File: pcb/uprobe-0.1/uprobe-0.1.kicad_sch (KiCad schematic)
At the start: 5 parts, among them J1 uConsoleEXT

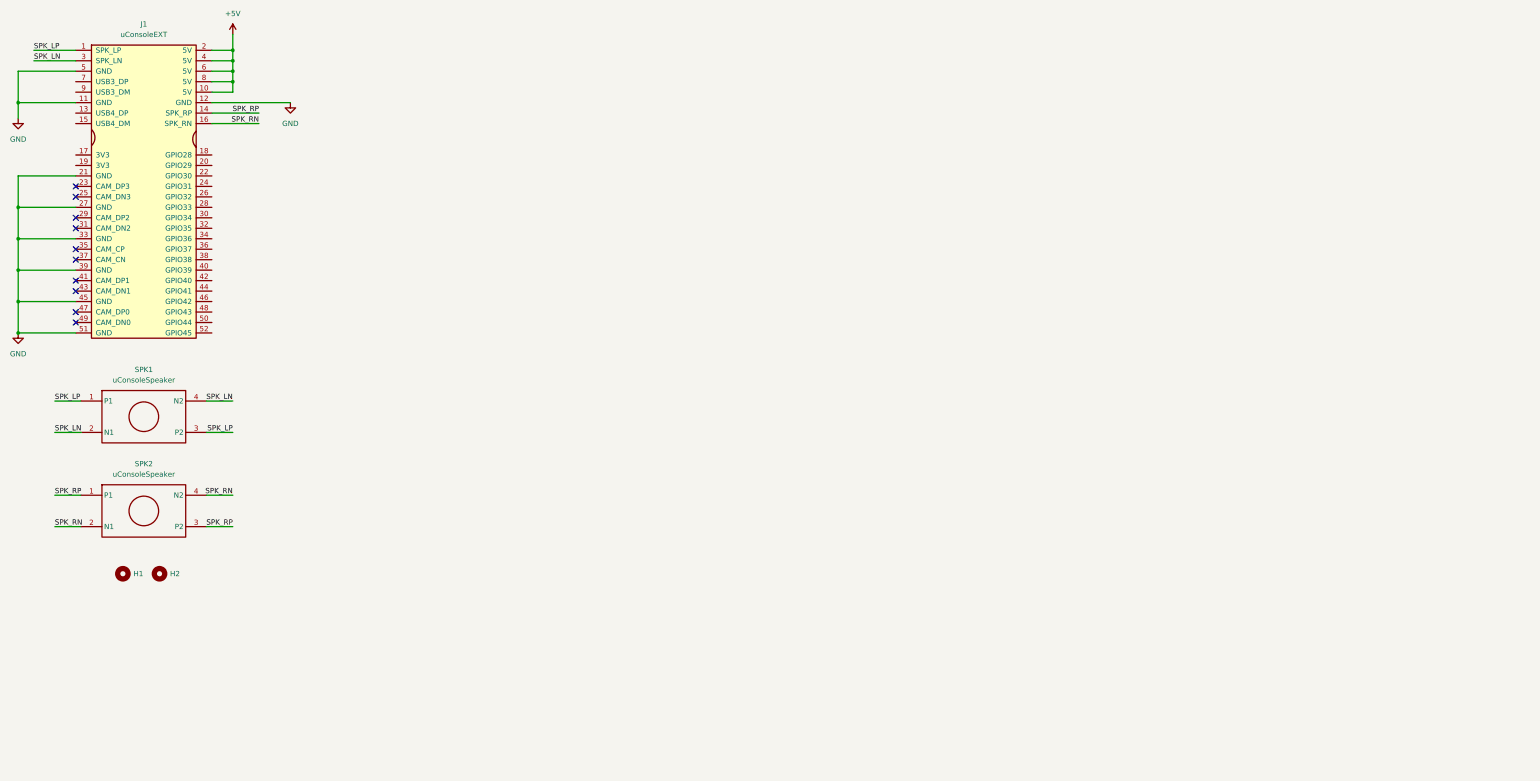
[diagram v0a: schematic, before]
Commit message: working on usbasp section
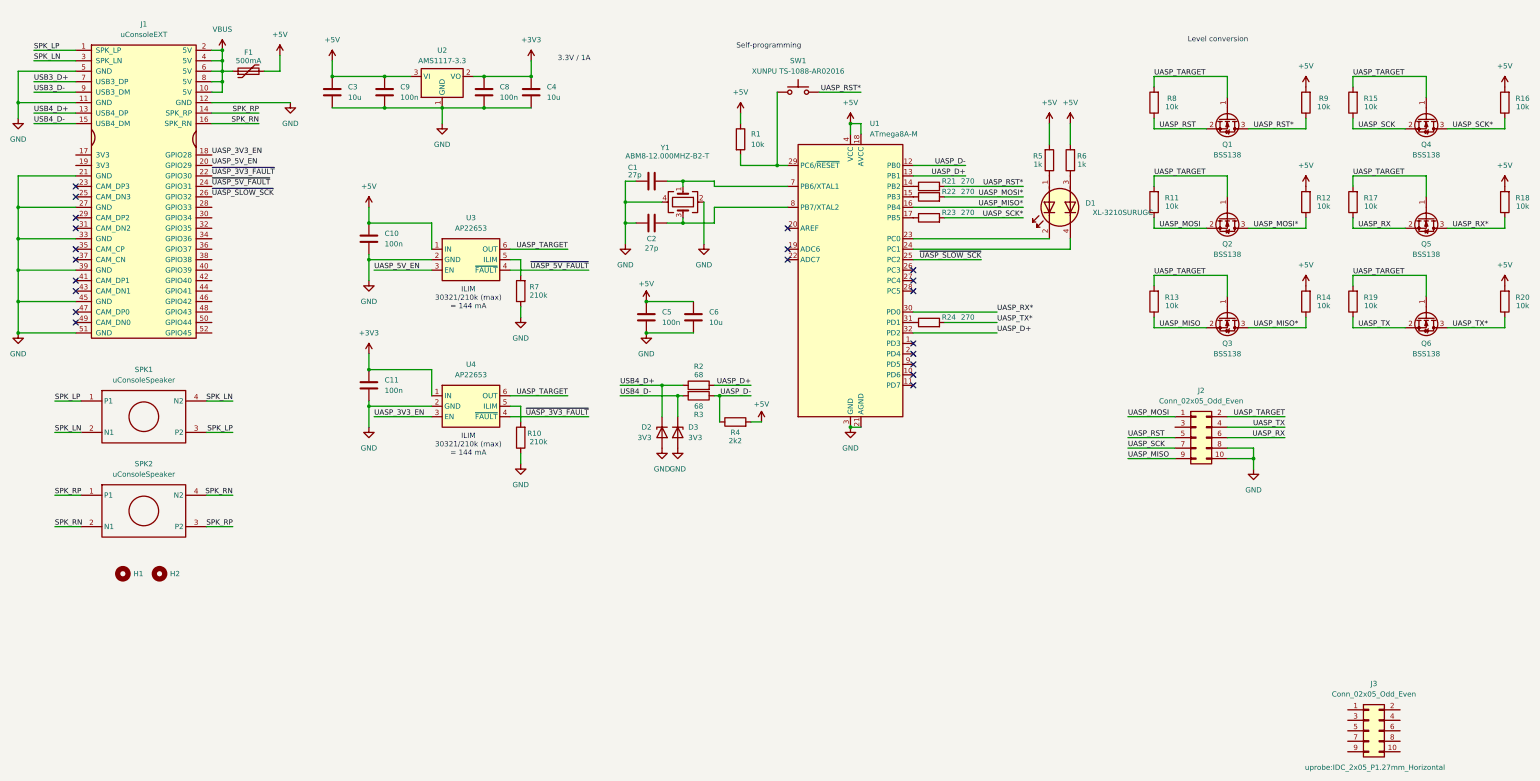
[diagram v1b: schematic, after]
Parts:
- added C1, C2: 27p, Capacitor_SMD:C_0603_1608Metric, symbol Device:C
- added C10, C11, C5, C8, C9: 100n, Capacitor_SMD:C_0603_1608Metric, symbol Device:C
- added C3, C4, C6: 10u, Capacitor_SMD:C_0805_2012Metric, symbol Device:C
- added D1: XL-3210SURUGC, uprobe:XL-3210SURUGC, symbol Device:LED_Dual_AKAK
- added D2, D3: 3V3, Diode_SMD:D_SOD-323, symbol Device:D_Zener
- added F1: 500mA, Fuse:Fuse_0805_2012Metric, symbol Device:Polyfuse
- added J2: Conn_02x05_Odd_Even, uprobe:IDC_2x05_SIDE, symbol Connector_Generic:Conn_02x05_Odd_Even
- added J3: Conn_02x05_Odd_Even, uprobe:IDC_2x05_P1.27mm_Horizontal, symbol Connector_Generic:Conn_02x05_Odd_Even
- added Q1, Q2, Q3, Q4, Q5, Q6: BSS138, Package_TO_SOT_SMD:SOT-23, symbol Transistor_FET:BSS138
- added R1, R11, R12, R13, R14, R15, R16, R17, R18, R19, R20, R8, R9: 10k, Resistor_SMD:R_0603_1608Metric, symbol Device:R
- added R10, R7: 210k, Resistor_SMD:R_0603_1608Metric, symbol Device:R
- added R2, R3: 68, Resistor_SMD:R_0603_1608Metric, symbol Device:R
- added R21, R22, R23, R24: 270, Resistor_SMD:R_0603_1608Metric, symbol Device:R
- added R4: 2k2, Resistor_SMD:R_0603_1608Metric, symbol Device:R
- added R5, R6: 1k, Resistor_SMD:R_0603_1608Metric, symbol Device:R
- added SW1: XUNPU TS-1088-AR02016, uprobe:XUNPU_TS-1088-AR02016, symbol Switch:SW_Push
- added U1: ATmega8A-M, Package_DFN_QFN:QFN-32-1EP_5x5mm_P0.5mm_EP3.1x3.1mm, symbol MCU_Microchip_ATmega:ATmega8A-M
- added U2: AMS1117-3.3, Package_TO_SOT_SMD:SOT-223-3_TabPin2, symbol Regulator_Linear:AMS1117-3.3
- added U3, U4: AP22653, Package_TO_SOT_SMD:SOT-23-6, symbol uprobe:AP22653
- added Y1: ABM8-12.000MHZ-B2-T, Crystal:Crystal_SMD_Abracon_ABM8G-4Pin_3.2x2.5mm, symbol Device:Crystal_GND24
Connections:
- net +5V: now also C10.1, C3.1, C5.1, C6.1, C9.1, F1.2, R1.1, R12.2, R14.2, R16.2, R18.2, R20.2, R4.2, R5.2, R6.2, R9.2, U1.18 (AVCC), U1.4 (VCC), U1.6 (VCC), U2.3 (VI), U3.1 (IN); no longer J1.10 (5V), J1.2 (5V), J1.4 (5V), J1.6 (5V), J1.8 (5V)
- net GND: now also C1.1, C10.2, C11.2, C2.1, C3.2, C4.2, C5.2, C6.2, C8.2, C9.2, D2.2 (A), D3.2 (A), J2.10 (Pin_10), J2.8 (Pin_8), R10.1, R7.1, U1.21 (AGND), U1.3 (GND), U1.33 (GND), U1.5 (GND), U2.1 (GND), U3.2 (GND), U4.2 (GND), Y1.2, Y1.4
- net USB4_D+: now reaches J1.13 (USB4_DP)
- net USB4_D+: now also D2.1 (K), R2.1
- net USB4_D-: now reaches J1.15 (USB4_DM)
- net USB4_D-: now also D3.1 (K), R3.2
- net UASP_3V3_EN: now reaches J1.18 (GPIO28)
- net UASP_3V3_EN: now also U4.3 (EN)
- net UASP_5V_EN: now reaches J1.20 (GPIO29)
- net UASP_5V_EN: now also U3.3 (EN)
- net ~{UASP_3V3_FAULT}: now reaches J1.22 (GPIO30)
- net ~{UASP_3V3_FAULT}: now also U4.4 (~{FAULT})
- net ~{UASP_5V_FAULT}: now reaches J1.24 (GPIO31)
- net ~{UASP_5V_FAULT}: now also U3.4 (~{FAULT})
- net ~{UASP_SLOW_SCK}: now reaches J1.26 (GPIO32)
- net ~{UASP_SLOW_SCK}: now also U1.25 (PC2)
- net USB3_D+: now reaches J1.7 (USB3_DP)
- net USB3_D-: now reaches J1.9 (USB3_DM)
- new net: R23.1, U1.17 (PB5)
- new net: R7.2, U3.5 (ILIM)
- new net: R1.2, SW1.1, U1.29 (PC6/~{RESET})
- new net: R10.2, U4.5 (ILIM)
- new net: C1.2, U1.7 (PB6/XTAL1), Y1.1
- new net: R24.1, U1.31 (PD1)
- new net: R22.1, U1.15 (PB3)
- new net: D1.1 (A1), R5.1
- new net: R21.1, U1.14 (PB2)
- new net: C2.2, U1.8 (PB7/XTAL2), Y1.3
- new net: D1.2 (K1), U1.23 (PC0)
- new net: D1.3 (A2), R6.1
- new net: D1.4 (K2), U1.24 (PC1)
- new net +3V3: C11.1, C4.1, C8.1, U2.2 (VO), U4.1 (IN)
- new net UASP_D+: R2.2, U1.13 (PB1), U1.32 (PD2)
- new net UASP_D-: R3.1, R4.1, U1.12 (PB0)
- new net UASP_MISO: J2.9 (Pin_9), Q3.2 (S), R13.1
- new net UASP_MISO*: Q3.3 (D), R14.1, U1.16 (PB4)
- new net UASP_MOSI: J2.1 (Pin_1), Q2.2 (S), R11.1
- new net UASP_MOSI*: Q2.3 (D), R12.1, R22.2
- new net UASP_RST: J2.5 (Pin_5), Q1.2 (S), R8.1
- new net UASP_RST*: Q1.3 (D), R21.2, R9.1, SW1.2
- new net UASP_RX: J2.6 (Pin_6), Q5.2 (S), R17.1
- new net UASP_RX*: Q5.3 (D), R18.1, U1.30 (PD0)
- new net UASP_SCK: J2.7 (Pin_7), Q4.2 (S), R15.1
- new net UASP_SCK*: Q4.3 (D), R16.1, R23.2
- new net UASP_TARGET: J2.2 (Pin_2), Q1.1 (G), Q2.1 (G), Q3.1 (G), Q4.1 (G), Q5.1 (G), Q6.1 (G), R11.2, R13.2, R15.2, R17.2, R19.2, R8.2, U3.6 (OUT), U4.6 (OUT)
- new net UASP_TX: J2.4 (Pin_4), Q6.2 (S), R19.1
- new net UASP_TX*: Q6.3 (D), R20.1, R24.2
- new net VBUS: F1.1, J1.10 (5V), J1.2 (5V), J1.4 (5V), J1.6 (5V), J1.8 (5V)
- no-connect marks 10 -> 21
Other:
- note added: "3.3V / 1A"
- note added: "ILIM 30321/210k (max) = 144 mA"
- note added: "Level conversion"
- note added: "Self-programming"

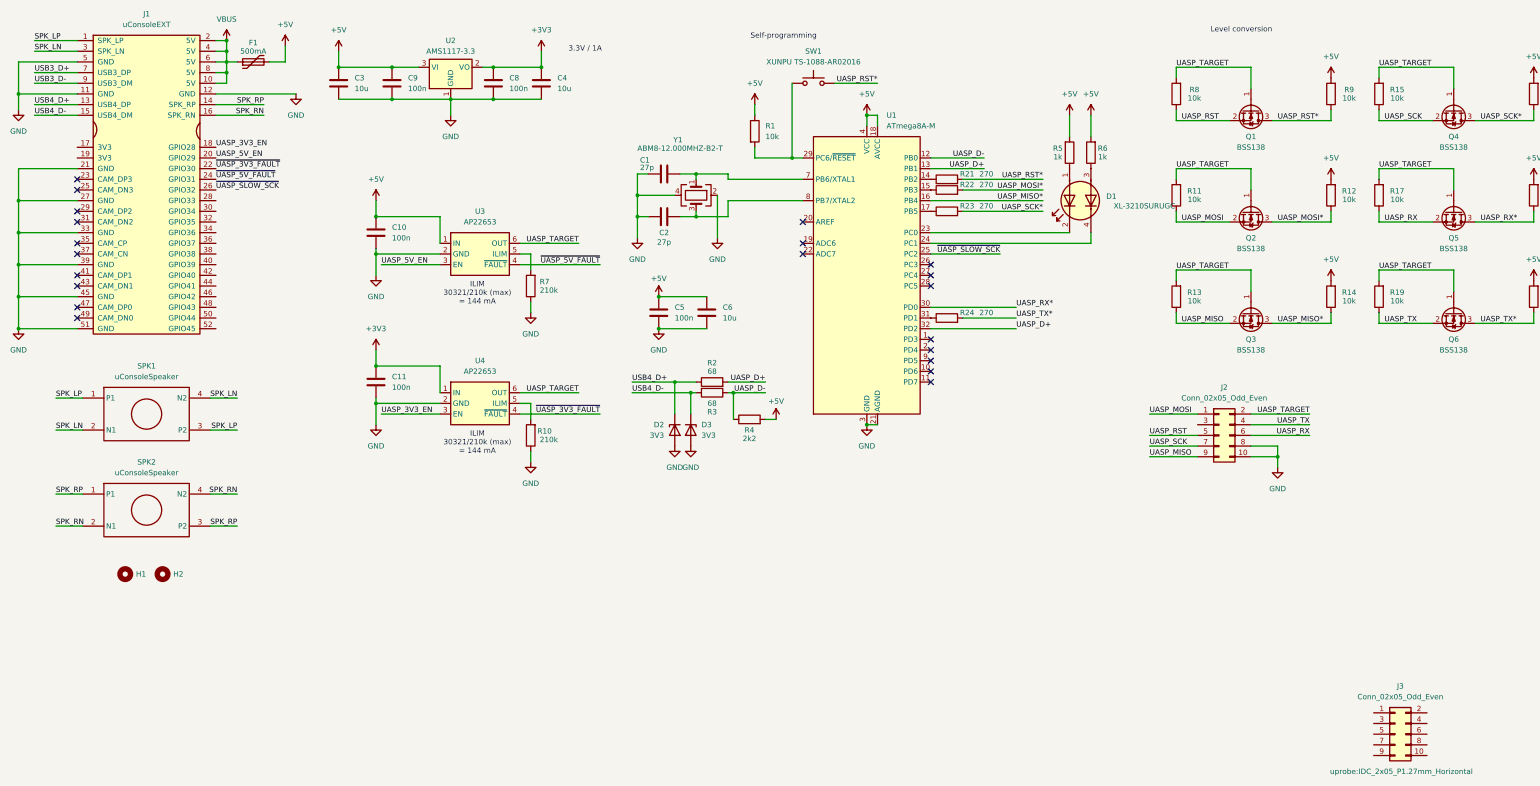
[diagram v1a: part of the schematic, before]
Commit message: add level shifter sim, schema in prog
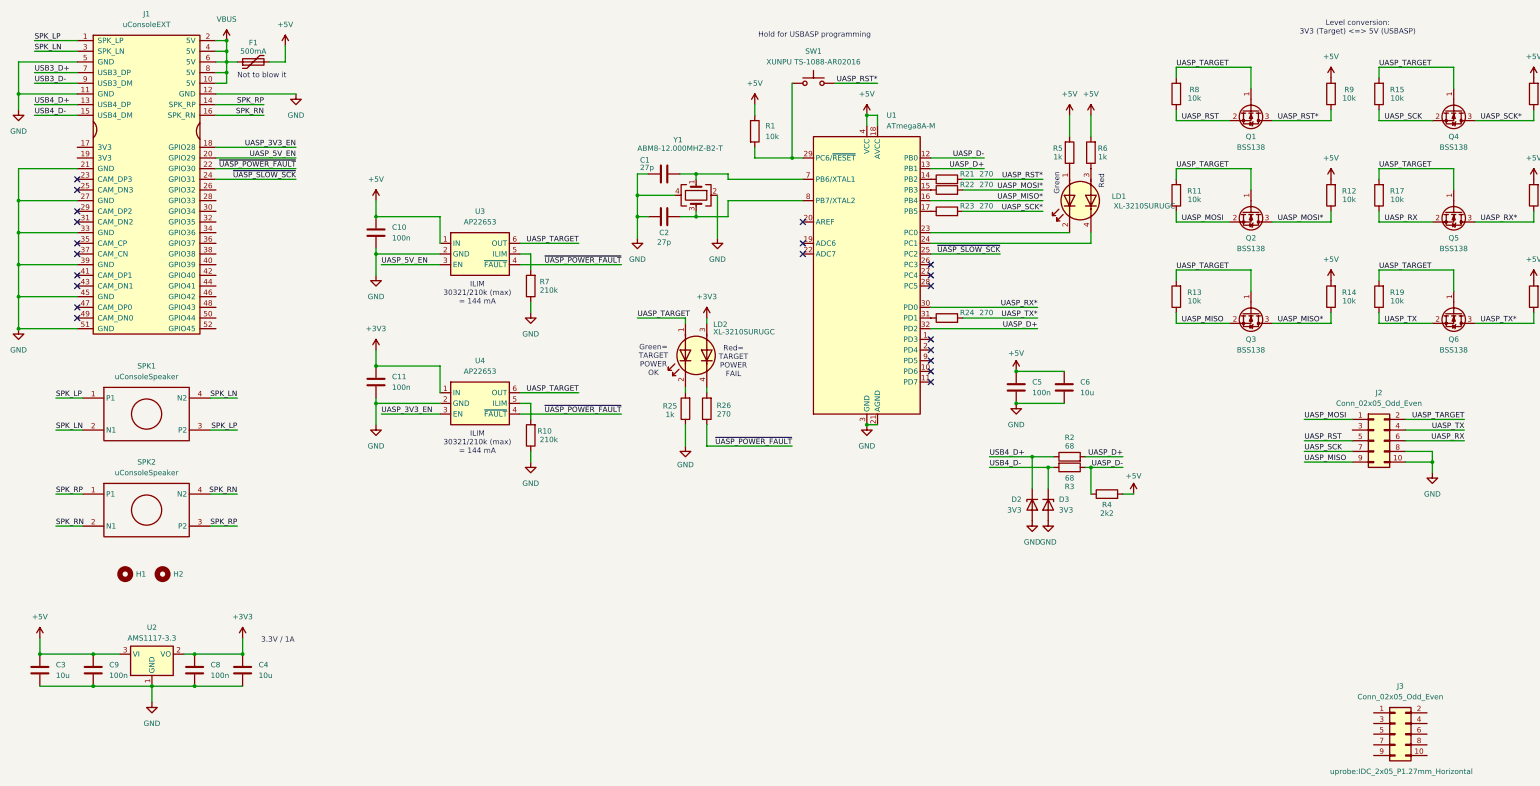
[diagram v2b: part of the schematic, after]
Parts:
- added LD2: XL-3210SURUGC, uprobe:XL-3210SURUGC, symbol Device:LED_Dual_AKAK
- added R25: 1k, Resistor_SMD:R_0603_1608Metric, symbol Device:R
- added R26: 270, Resistor_SMD:R_0603_1608Metric, symbol Device:R
- renumbered D1 to LD1
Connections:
- net +3V3: now also LD2.3 (A2)
- net GND: now also R25.1
- net UASP_TARGET: now also LD2.1 (A1)
- net ~{UASP_SLOW_SCK}: now also J1.24 (GPIO31); no longer J1.26 (GPIO32)
- net ~{UASP_3V3_FAULT} renamed ~{UASP_POWER_FAULT}
- net ~{UASP_POWER_FAULT}: now also U3.4 (~{FAULT}), R26.1
- removed net ~{UASP_5V_FAULT}: J1.24 (GPIO31), U3.4 (~{FAULT})
- new net: LD2.2 (K1), R25.2
- new net: LD2.4 (K2), R26.2
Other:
- note added: "Green"
- note added: "Green= TARGET POWER OK"
- note added: "Hold for USBASP programming"
- note added: "Level conversion: 3V3 (Target) <=> 5V (USBASP)"
- note added: "Not to blow it"
- note added: "Red"
- note added: "Red= TARGET POWER FAIL"
- note removed: "Level conversion"
- note removed: "Self-programming"
- moved on the sheet: C3, C4, C5, C6, C8, C9, D2, D3, J2, R2, R3, R4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

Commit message: add bmp schematics
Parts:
- added C12, C13, C14, C15, C16, C17, C18, C21, C22, C23, C24, C25, C26, C27, C28: 100n, Capacitor_SMD:C_0603_1608Metric, symbol Device:C
- added C19, C20: 27p, Capacitor_SMD:C_0603_1608Metric, symbol Device:C
- added C7: 10u, Capacitor_SMD:C_0805_2012Metric, symbol Device:C
- added J4: JST_SH_BM03B-SRSS, Connector_JST:JST_SH_BM03B-SRSS-TB_1x03-1MP_P1.00mm_Vertical, symbol Connector_Generic_MountingPin:Conn_01x03_MountingPin
- added J5: Conn_01x02, Connector_PinHeader_2.54mm:PinHeader_1x02_P2.54mm_Vertical, symbol Connector_Generic:Conn_01x02
- added J7: Conn_01x04, Connector_PinHeader_2.54mm:PinHeader_1x04_P2.54mm_Vertical, symbol Connector_Generic:Conn_01x04
- added JP1: SolderJumper_2_Open, Jumper:SolderJumper-2_P1.3mm_Open_TrianglePad1.0x1.5mm, symbol Jumper:SolderJumper_2_Open
- added Q7: DMG1024UV, Package_TO_SOT_SMD:SOT-563, symbol Transistor_FET:Q_Dual_NMOS_S1G1D2S2G2D1
- added Q8: DMG1023UV, Package_TO_SOT_SMD:SOT-563, symbol Transistor_FET:Q_Dual_PMOS_S1G1D2S2G2D1
- added R27, R28: 22, Resistor_SMD:R_0603_1608Metric, symbol Device:R
- added R29: 1k5, Resistor_SMD:R_0603_1608Metric, symbol Device:R
- added R30, R32, R33: 4k7, Resistor_SMD:R_0603_1608Metric, symbol Device:R
- added R31, R34, R35, R36: 10k, Resistor_SMD:R_0603_1608Metric, symbol Device:R
- added RN1, RN2: 100, Resistor_SMD:R_Array_Concave_4x0603, symbol Device:R_Pack04
- added SW2: XUNPU TS-1088-AR02016, uprobe:XUNPU_TS-1088-AR02016, symbol Switch:SW_Push
- added U5: STM32F103CBUx, Package_DFN_QFN:QFN-48-1EP_7x7mm_P0.5mm_EP5.6x5.6mm, symbol MCU_ST_STM32F1:STM32F103CBUx
- added U6, U7, U8, U9: 74LVC2T45DC, Package_SO:VSSOP-8_2.3x2mm_P0.5mm, symbol Logic_LevelTranslator:74LVC2T45DC
- added Y2: ABM8-8.000MHZ-B2-T, Crystal:Crystal_SMD_Abracon_ABM8G-4Pin_3.2x2.5mm, symbol Device:Crystal_GND24
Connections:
- net +3V3: now also C13.1, C14.1, C15.1, C16.1, C17.1, C21.1, C23.1, C25.1, C27.1, C7.1, Q8.6 (D), R32.2, U5.1 (VBAT), U5.24 (VDD), U5.36 (VDD), U5.40 (PB4), U5.41 (PB5), U5.42 (PB6), U5.48 (VDD), U5.9 (VDDA), U6.1 (VCCA), U6.5 (DIR), U7.1 (VCCA), U7.5 (DIR), U8.1 (VCCA), U9.1 (VCCA)
- net +5V: now also J5.1 (Pin_1), R30.2
- net GND: now also J3.3 (Pin_3), J3.5 (Pin_5), J3.9 (Pin_9), C12.2, C13.2, C14.2, C15.2, C16.2, C17.2, C18.2, C19.1, C20.1, C21.2, C22.2, C23.2, C24.2, C25.2, C26.2, C27.2, C28.2, C7.2, J4.2 (Pin_2), J4.MP (MountPin), J5.2 (Pin_2), J7.4 (Pin_4), Q7.1 (S), Q7.4 (S), R31.1, R34.1, SW2.1, U5.23 (VSS), U5.35 (VSS), U5.44 (BOOT0), U5.47 (VSS), U5.49 (VSS), U5.8 (VSSA), U6.2 (1A), U6.4 (GND), U6.7 (1B), U7.4 (GND), U8.4 (GND), U8.5 (DIR), U9.2 (1A), U9.4 (GND), U9.7 (1B), Y2.2, Y2.4
- net USB3_D+: now also R28.1, R29.2
- net USB3_D-: now also R27.2
- net TPWR: now reaches J3.1 (Pin_1)
- net TPWR: now also Q8.3 (D), R33.2, RN2.6 (R3.2)
- net RST: now reaches J3.10 (Pin_10)
- net RST: now also RN2.5 (R4.2)
- net TMS: now reaches J3.2 (Pin_2)
- net TMS: now also RN1.5 (R4.2)
- net TCK: now reaches J3.4 (Pin_4)
- net TCK: now also RN1.6 (R3.2)
- net TDO: now reaches J3.6 (Pin_6)
- net TDO: now also RN1.7 (R2.2)
- net TDI: now reaches J3.8 (Pin_8)
- net TDI: now also RN1.8 (R1.2)
- new net: C19.2, U5.5 (PD0), Y2.1
- new net: R29.1, U5.29 (PA8)
- new net: C18.1, R33.1, R34.2, U5.18 (PB0)
- new net: C20.2, U5.6 (PD1), Y2.3
- new net: R32.1, SW2.2, U5.25 (PB12)
- new net: Q8.1 (S), Q8.4 (S), R36.2
- new net BM_D+: R28.2, U5.33 (PA12)
- new net BM_D-: R27.1, U5.32 (PA11)
- new net BM_LED0: U5.20 (PB2)
- new net BM_LED1: U5.21 (PB10)
- new net BM_LED2: U5.22 (PB11)
- new net BM_SWCLK: J7.3 (Pin_3), U5.37 (PA14)
- new net BM_SWDIO: J7.2 (Pin_2), U5.34 (PA13)
- new net PWR_BR: Q8.2 (G), Q8.5 (G), R36.1, U5.19 (PB1)
- new net RXD: J4.1 (Pin_1), RN2.7 (R2.2)
- new net TRACESWO: U5.39 (PB3)
- new net TRSWO: JP1.2 (B), U5.43 (PB7)
- new net TXD: J4.3 (Pin_3), RN2.8 (R1.2)
- new net VBUS_DTCT: R30.1, R31.2, U5.26 (PB13)
- new net iRST: Q7.2 (G), U5.12 (PA2)
- new net iRST_SENSE: Q7.3 (D), U5.17 (PA7)
- new net iRXD: U5.31 (PA10), U8.3 (2A)
- new net iTCK: U5.15 (PA5), U7.2 (1A)
- new net iTDI: U5.13 (PA3), U7.3 (2A)
- new net iTDO: JP1.1 (A), U5.16 (PA6), U8.2 (1A)
- new net iTMS: U5.14 (PA4), U9.3 (2A)
- new net iTMS_DIR: U5.11 (PA1), U9.5 (DIR)
- new net iTXD: U5.30 (PA9), U6.3 (2A)
- new net xRST: Q7.5 (G), Q7.6 (D), R35.1, RN2.4 (R4.1)
- new net xRXD: RN2.2 (R2.1), U8.6 (2B)
- new net xTCK: RN1.3 (R3.1), U7.7 (1B)
- new net xTDI: RN1.1 (R1.1), U7.6 (2B)
- new net xTDO: RN1.2 (R2.1), U8.7 (1B)
- new net xTMS: RN1.4 (R4.1), U9.6 (2B)
- new net xTPWR: C22.1, C24.1, C26.1, C28.1, R35.2, RN2.3 (R3.1), U6.8 (VCCB), U7.8 (VCCB), U8.8 (VCCB), U9.8 (VCCB)
- new net xTXD: RN2.1 (R1.1), U6.6 (2B)
- new net ~{BM_RST}: C12.1, J7.1 (Pin_1), U5.7 (NRST)
- no-connect marks 21 -> 31
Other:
- note added: "<- DIR = GND -> DIR = VCC"
- note added: "BM HW Version"
- note added: "BMPM2"
- note added: "COMMON"
- note added: "TODO: LEDS!!!"
- note added: "USBASP"
- moved on the sheet: C1, C10, C11, C2, C3, C4, C5, C6, C8, C9, D2, D3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

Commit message: update usbasp schema
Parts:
- removed Q2, Q3, Q4, Q5, Q6: BSS138, Package_TO_SOT_SMD:SOT-23, symbol Transistor_FET:BSS138
- removed R11, R12, R13, R14, R15, R16, R17, R18, R19, R20: 10k, Resistor_SMD:R_0603_1608Metric, symbol Device:R
- removed R21, R22, R23, R24: 270, Resistor_SMD:R_0603_1608Metric, symbol Device:R
- added C29, C30, C31, C32, C33, C34: 100n, Capacitor_SMD:C_0603_1608Metric, symbol Device:C
- added R37, R38, R39, R40, R41, R42: 100, Resistor_SMD:R_0603_1608Metric, symbol Device:R
- added U10, U11, U12: 74LVC2T45DC, Package_SO:VSSOP-8_2.3x2mm_P0.5mm, symbol Logic_LevelTranslator:74LVC2T45DC
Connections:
- net +5V: now also C29.1, C31.1, C33.1, U10.1 (VCCA), U10.5 (DIR), U11.1 (VCCA), U11.5 (DIR), U12.1 (VCCA)
- net GND: now also C29.2, C30.2, C31.2, C32.2, C33.2, C34.2, U10.4 (GND), U11.2 (1A), U11.4 (GND), U11.7 (1B), U12.4 (GND), U12.5 (DIR)
- net UASP_MISO: now also R42.1, U12.7 (1B); no longer J2.9 (Pin_9)
- net UASP_MISO*: now also U12.2 (1A)
- net UASP_MOSI: now also R39.1, U10.7 (1B); no longer J2.1 (Pin_1)
- net UASP_MOSI*: now also U1.15 (PB3), U10.2 (1A)
- net UASP_RST: now also R8.2, R40.1; no longer J2.5 (Pin_5), R8.1
- net UASP_RST*: now also U1.14 (PB2)
- net UASP_RX: now also R37.2, U12.6 (2B); no longer J2.6 (Pin_6)
- net UASP_RX*: now also U12.3 (2A)
- net UASP_SCK: now also R41.1, U11.6 (2B); no longer J2.7 (Pin_7)
- net UASP_SCK*: now also U1.17 (PB5), U11.3 (2A)
- net UASP_TARGET: now also R8.1, C30.1, C32.1, C34.1, U10.8 (VCCB), U11.8 (VCCB), U12.8 (VCCB); no longer R8.2
- net UASP_TX: now also R38.2, U10.6 (2B); no longer J2.4 (Pin_4)
- net UASP_TX*: now also U1.31 (PD1), U10.3 (2A)
- new net: J2.7 (Pin_7), R41.2
- new net: J2.4 (Pin_4), R38.1
- new net: J2.5 (Pin_5), R40.2
- new net: J2.9 (Pin_9), R42.2
- new net: J2.1 (Pin_1), R39.2
- new net: J2.6 (Pin_6), R37.1
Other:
- note added: "Level conversion: 5V (USBASP) <=> 3V3 (Target)"
- note removed: "Level conversion: 3V3 (Target) <=> 5V (USBASP)"
- moved on the sheet: C5, C6, D2, D3, J2, Q1, R2, R3, R4, R8, R9
